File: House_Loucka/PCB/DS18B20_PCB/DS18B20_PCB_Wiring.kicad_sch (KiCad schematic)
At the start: 7 parts, among them J1 Conn_01x02_Socket_data, J2 Conn_01x02_Socke_Voltage, J3 Conn_01x02_Socket_GND, J4 Conn_01x03_Socket, U1 DS18B20, U2 DS18B20

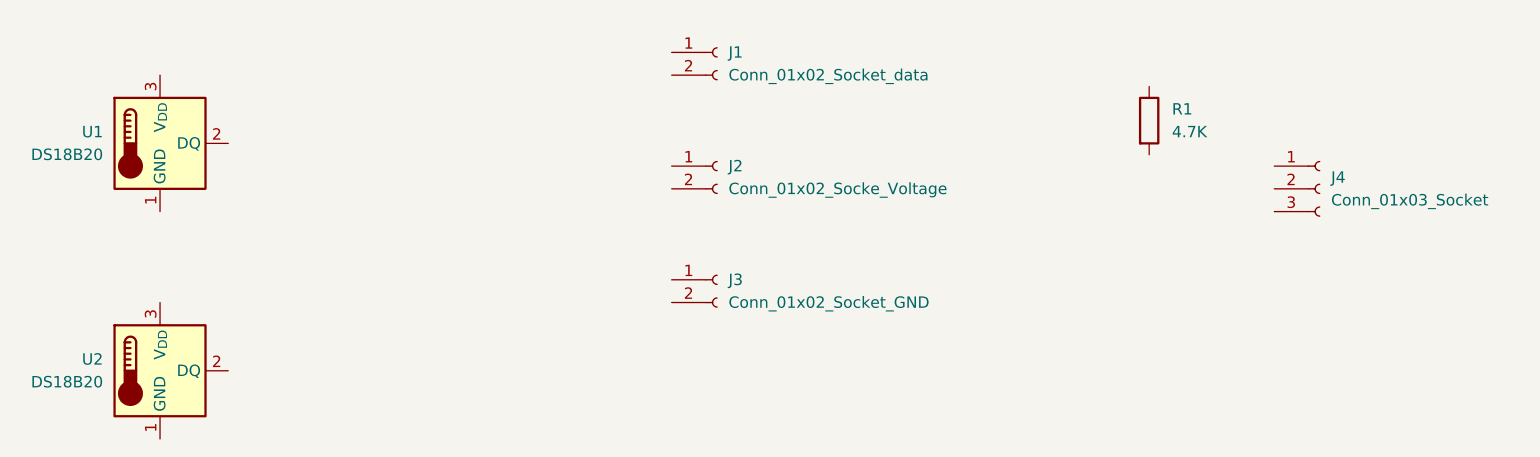
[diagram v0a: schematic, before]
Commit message: Update PCB DS18B20 tables updated
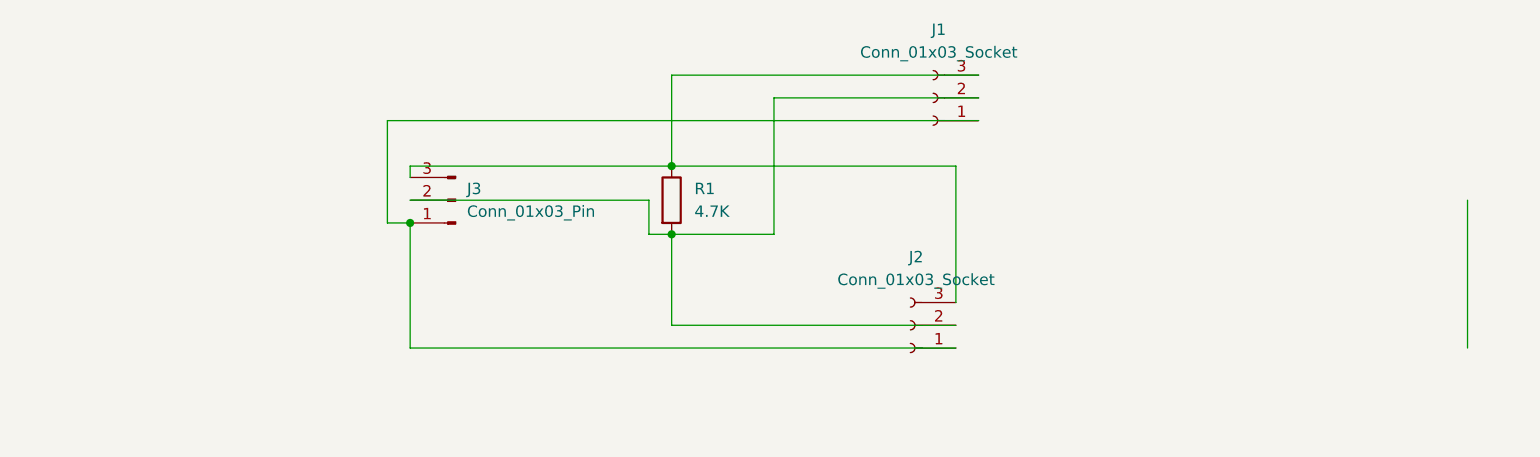
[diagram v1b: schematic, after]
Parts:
- removed J1: Conn_01x02_Socket_data, symbol Connector:Conn_01x02_Socket
- removed J2: Conn_01x02_Socke_Voltage, symbol Connector:Conn_01x02_Socket
- removed J3: Conn_01x02_Socket_GND, symbol Connector:Conn_01x02_Socket
- removed J4: Conn_01x03_Socket, symbol Connector:Conn_01x03_Socket
- removed U1, U2: DS18B20, Package_TO_SOT_THT:TO-92_Inline, symbol Sensor_Temperature:DS18B20
- added J1, J2: Conn_01x03_Socket, Connector_PinSocket_2.54mm:PinSocket_1x03_P2.54mm_Vertical, symbol Connector:Conn_01x03_Socket
- added J3: Conn_01x03_Pin, Connector_PinSocket_2.54mm:PinSocket_1x03_P2.54mm_Vertical, symbol Connector:Conn_01x03_Pin
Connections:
- net at R1.1: now also J1.3 (Pin_3), J2.3 (Pin_3), J3.3 (Pin_3)
- net at R1.2: now also J1.2 (Pin_2), J2.2 (Pin_2), J3.2 (Pin_2)
- new net: J1.1 (Pin_1), J2.1 (Pin_1), J3.1 (Pin_1)
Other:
- moved on the sheet: R1
